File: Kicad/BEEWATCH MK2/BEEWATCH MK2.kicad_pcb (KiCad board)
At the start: 2 copper layers, 40.3 x 39.7 mm, 117 parts, among them IC1 LTC3549EDCB#TRMPBF, J1 USB_C_Receptacle_USB2.0, J3 Conn_02x06_Odd_Even, Q1 DMG6968U, Q2 DMG6968U, Q3 DMP1045U-7, Q4 DMG6968U, Q5 BSS138, Q6 BSS138, Q7 BSS138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

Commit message: minor changes
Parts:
- moved D1 6.40 mm to (168.7, 104.9), turned to 180 degrees
- moved R6 2.77 mm to (166.6, 105.0), turned to 90 degrees
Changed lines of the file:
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@@
 		(tags "SOT TO_SOT_SMD")
 		(property "Reference" "Q8"
-			(at -16.0375 -47.75 90)
+			(at 1.6 -2 90)
 			(layer "F.SilkS")
 			(effects
@@
 	(footprint "Resistor_SMD:R_0402_1005Metric_Pad0.72x0.64mm_HandSolder"
 		(layer "B.Cu")
-		(at 168.464645 107.05 180)
+		(at 166.6 105 90)
 		(descr "Resistor SMD 0402 (1005 Metric), square (rectangular) end terminal, IPC_7351 nominal with elongated pad for handsoldering. (Body size source: IPC-SM-782 page 72, https://www.pcb-3d.com/wordpress/wp-content/uploads/ipc-sm-782a_amendment_1_and_2.pdf), generated with kicad-footprint-generator")
 		(tags "resistor handsolder")
 		(property "Reference" "R6"
-			(at 0 1.17 0)
+			(at 0 1.17 90)
 			(layer "B.SilkS")
 			(effects
@@
 		)
 		(property "Value" "1K"
-			(at 0 -1.17 0)
+			(at 0 -1.17 90)
 			(layer "B.Fab")
 			(effects
@@
 		)
 		(property "Footprint" "Resistor_SMD:R_0402_1005Metric_Pad0.72x0.64mm_HandSolder"
-			(at 0 0 0)
+			(at 0 0 -90)
 			(unlocked yes)
 			(layer "B.Fab")
@@
 		)
 		(property "Datasheet" ""
-			(at 0 0 0)
+			(at 0 0 -90)
 			(unlocked yes)
 			(layer "B.Fab")
@@
 		)
 		(property "Description" "Resistor, small symbol"
-			(at 0 0 0)
+			(at 0 0 -90)
 			(unlocked yes)
 			(layer "B.Fab")
@@
 		(attr smd)
 		(fp_line
-			(start 0.167621 0.38)
-			(end -0.167621 0.38)
+			(start 0.167621 -0.380001)
+			(end -0.167621 -0.380001)
 			(stroke
 				(width 0.12)
@@
 		)
 		(fp_line
-			(start 0.167621 -0.38)
-			(end -0.167621 -0.38)
+			(start 0.167621 0.380001)
+			(end -0.167621 0.380001)
 			(stroke
 				(width 0.12)
@@
 		)
 		(fp_line
-			(start 1.1 0.47)
-			(end -1.1 0.47)
+			(start 1.1 -0.47)
+			(end 1.1 0.47)
 			(stroke
 				(width 0.05)
@@
 		)
 		(fp_line
-			(start 1.1 -0.47)
-			(end 1.1 0.47)
+			(start -1.1 -0.47)
+			(end 1.1 -0.47)
 			(stroke
 				(width 0.05)
@@
 		)
 		(fp_line
-			(start -1.1 0.47)
-			(end -1.1 -0.47)
+			(start 1.1 0.47)
+			(end -1.1 0.47)
 			(stroke
 				(width 0.05)
@@
 		)
 		(fp_line
-			(start -1.1 -0.47)
-			(end 1.1 -0.47)
+			(start -1.1 0.47)
+			(end -1.1 -0.47)
 			(stroke
 				(width 0.05)
@@
 		)
 		(fp_line
-			(start 0.525 0.27)
-			(end -0.525 0.27)
+			(start 0.525 -0.27)
+			(end 0.525 0.27)
 			(stroke
 				(width 0.1)
@@
 		)
 		(fp_line
-			(start 0.525 -0.27)
-			(end 0.525 0.27)
+			(start -0.525 -0.27)
+			(end 0.525 -0.27)
 			(stroke
 				(width 0.1)
@@
 		)
 		(fp_line
-			(start -0.525 0.27)
-			(end -0.525 -0.27)
+			(start 0.525 0.27)
+			(end -0.525 0.27)
 			(stroke
 				(width 0.1)
@@
 		)
 		(fp_line
-			(start -0.525 -0.27)
-			(end 0.525 -0.27)
+			(start -0.525 0.27)
+			(end -0.525 -0.27)
 			(stroke
 				(width 0.1)
@@
 		)
 		(fp_text user "${REFERENCE}"
-			(at 0 0 0)
+			(at 0 0 90)
 			(layer "B.Fab")
 			(effects
@@
 		)
 		(pad "1" smd roundrect
-			(at -0.5975 0 180)
+			(at -0.5975 0 90)
 			(size 0.715 0.64)
 			(layers "B.Cu" "B.Paste" "B.Mask")
@@
 		)
 		(pad "2" smd roundrect
-			(at 0.5975 0 180)
+			(at 0.5975 0 90)
 			(size 0.715 0.64)
 			(layers "B.Cu" "B.Paste" "B.Mask")
@@
 	(footprint "SM_LED:XL-0807RGBC-WS2812B"
 		(layer "B.Cu")
-		(at 167.1 111.1)
+		(at 168.7 104.9 180)
 		(property "Reference" "D1"
-			(at 0.5 1.7 180)
+			(at 0.5 1.7 0)
 			(unlocked yes)
 			(layer "B.SilkS")
@@
 		)
 		(property "Value" "WS2812B"
-			(at 0 -1 180)
+			(at 0 -1 0)
 			(unlocked yes)
 			(layer "B.Fab")
@@
 		)
 		(property "Footprint" "SM_LED:XL-0807RGBC-WS2812B"
-			(at 0 0 180)
+			(at 0 0 0)
 			(unlocked yes)
 			(layer "B.Fab")
@@
 		)
 		(property "Datasheet" "https://cdn-shop.adafruit.com/datasheets/WS2812B.pdf"
-			(at 0 0 180)
+			(at 0 0 0)
 			(unlocked yes)
 			(layer "B.Fab")
@@
 		)
 		(property "Description" "RGB LED with integrated controller"
-			(at 0 0 180)
+			(at 0 0 0)
 			(unlocked yes)
 			(layer "B.Fab")
@@
 		(attr smd)
 		(fp_line
-			(start 0.75 -0.9)
-			(end -0.75 -0.9)
+			(start 0.75 0.9)
+			(end -0.75 0.9)
 			(stroke
 				(width 0.1)
@@
 		)
 		(fp_line
-			(start 0.75 0.9)
-			(end -0.75 0.9)
+			(start 0.75 -0.9)
+			(end -0.75 -0.9)
 			(stroke
 				(width 0.1)
@@
 			(layer "B.SilkS")
 		)
-		(fp_rect
-			(start -1.15 1.05)
-			(end 1.15 -1.05)
+		(fp_poly
+			(pts
+				(xy -1.15 1.05) (xy 1.15 1.05) (xy 1.15 -1.05) (xy -1.15 -1.05)
+			)
 			(stroke
 				(width 0.05)
@@
 		)
 		(fp_text user "${REFERENCE}"
-			(at 0 -2.5 180)
+			(at 0 -2.5 0)
 			(unlocked yes)
 			(layer "B.Fab")
@@
 		)
 		(pad "1" smd roundrect
-			(at 0.75 0.45)
+			(at 0.75 0.45 180)
 			(size 0.6 0.7)
 			(layers "B.Cu" "B.Paste" "B.Mask")
@@
 		)
 		(pad "2" smd roundrect
-			(at -0.75 0.45)
+			(at -0.75 0.45 180)
 			(size 0.6 0.7)
 			(layers "B.Cu" "B.Paste" "B.Mask")
@@
 		)
 		(pad "3" smd roundrect
-			(at -0.75 -0.45)
+			(at -0.75 -0.45 180)
 			(size 0.6 0.7)
 			(layers "B.Cu" "B.Paste" "B.Mask")
@@
 		)
 		(pad "4" smd roundrect
-			(at 0.75 -0.45)
+			(at 0.75 -0.45 180)
 			(size 0.6 0.7)
 			(layers "B.Cu" "B.Paste" "B.Mask")
@@
 			(pintype "input")
 		)
-		(model "/home/krishnawa/git/BEEWATCH/3D/LED/XL-0807RGBC-WS2812B.step"
+		(model "${KIPRJMOD}/KiCadoodle/LIB/SM_LED/3D/0807RGB/XL-0807RGBC-WS2812B.step"
 			(offset
 				(xyz 0 0 0)
@@
 			(pintype "passive")
 		)
-		(model "/home/krishnawa/git/BEEWATCH/3D/SWITCH/Tact Switch-TK-074-4 Pin SMD.step"
+		(model "${KIPRJMOD}/KiCadoodle/LIB/SM_SWITCH/3D/TK-074/Tact Switch-TK-074-4 Pin SMD.step"
 			(offset
 				(xyz 0 0 0)
@@
 			(pintype "passive")
 		)
-		(model "/home/krishnawa/git/BEEWATCH/3D/SWITCH/Tact Switch-TK-074-4 Pin SMD.step"
+		(model "${KIPRJMOD}/KiCadoodle/LIB/SM_SWITCH/3D/TK-074/Tact Switch-TK-074-4 Pin SMD.step"
 			(offset
 				(xyz 0 0 0)

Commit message: Update
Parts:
- moved R22 11.5 mm to (133.8, 100.8), turned to 0 degrees
- moved R21 9.19 mm to (133.8, 102.2), turned to 0 degrees
- moved R2 8.52 mm to (139.9, 103.3), turned to 0 degrees
- moved R1 8.03 mm to (139.9, 106.3), turned to 0 degrees
- moved R20 3.82 mm to (137.4, 102.0), turned to 0 degrees
- moved R37 2.06 mm to (149.2, 98.4), turned to 0 degrees
- moved R36 0.30 mm to (145.9, 99.5)
- moved C22 0.21 mm to (132.8, 97.8)
- moved R43 0.20 mm to (140.9, 97.2)
- moved C23 0.19 mm to (134.3, 97.8)
- moved R33 0.18 mm to (141.7, 102.9)
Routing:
- net VBUS: track 0.00 -> 25.5 mm
- net /Battery&BMS/VBAT: track 0.00 -> 19.3 mm
- net /Battery&BMS/+VBAT_IN: track 0.00 -> 12.6 mm
- net GND: track 0.00 -> 10.6 mm, vias 0 -> 3
- net +3.3V: track 0.00 -> 5.57 mm, vias 0 -> 2
- net Net-(J1-CC1): track 0.00 -> 4.02 mm
- net Net-(U4-STAT): track 0.00 -> 3.17 mm
- net /ESP32/D+: track 0.00 -> 2.83 mm
- net /ESP32/D-: track 0.00 -> 2.78 mm
- net Net-(J1-CC2): track 0.00 -> 2.70 mm
- net /ESP32/XTAL_32K_P: track 0.00 -> 1.11 mm
- net /Battery&BMS/+3V3_IN: track 0.00 -> 0.99 mm
- added copper zone on In2.Cu, net +3.3V
- added copper zone on In1.Cu, net GND
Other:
- copper layers 2 -> 4

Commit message: ERC Checking
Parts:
- moved R23 1.49 mm to (154.7, 113.6)
- moved Y1 0.13 mm to (155.1, 116.0), turned to -45 degrees
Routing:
- net Net-(U1-GPIO46): track 0.00 -> 10.9 mm, vias 0 -> 2
- net Net-(U1-GPIO45): track 0.00 -> 9.92 mm, vias 0 -> 2
- net /ESP32/U1TXD: track 0.00 -> 9.46 mm, vias 0 -> 2
- net /ESP32/U1RXD: track 0.00 -> 6.76 mm, vias 0 -> 2
- net /ESP32/XTAL_P: track 0.00 -> 5.26 mm
- net /ESP32/XTAL_N: track 0.50 -> 5.34 mm
- net /ACCELEROMETER/MPU_SDA: track 0.00 -> 4.46 mm
- net 3V3: track 0.00 -> 4.38 mm
- net /ESP32/XTAL_32K_N: track 0.00 -> 4.38 mm
- net /ESP32/USB_D+: track 0.00 -> 3.97 mm
- net /ESP32/USB_D-: track 0.00 -> 3.94 mm
- net VDD3P3_RTC: track 0.00 -> 3.53 mm
- net /ESP32/D-: track 2.78 -> 0.00 mm
- net /ESP32/XTAL_32K_P: track 1.11 -> 3.34 mm
- net /ACCELEROMETER/MPU_SCL: track 0.00 -> 2.01 mm
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
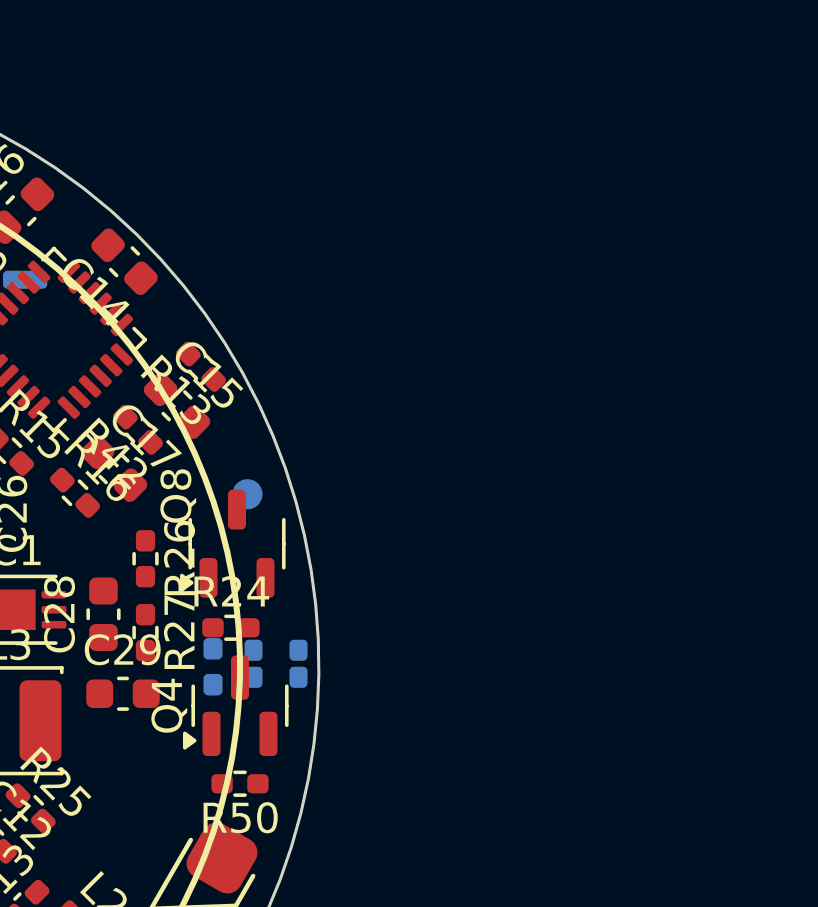
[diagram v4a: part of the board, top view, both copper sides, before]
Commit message: ERC going on anf All Lib issue is fixed
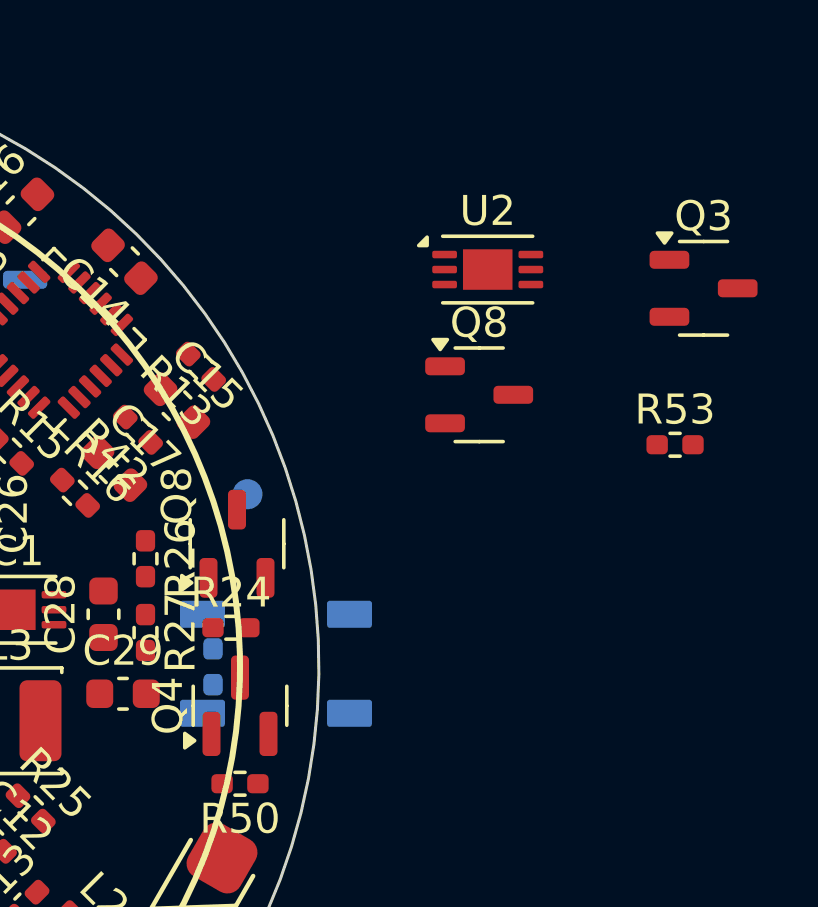
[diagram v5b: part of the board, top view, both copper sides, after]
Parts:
- added Q3: DMP1045U-7, Package_TO_SOT_SMD:SOT-23-3, F.Cu at (183.0, 92.4)
- added Q8: DMP1045U-7, Package_TO_SOT_SMD:SOT-23-3, F.Cu at (175.5, 95.9)
- added R53: 0, Resistor_SMD:R_0402_1005Metric_Pad0.72x0.64mm_HandSolder, F.Cu at (182.0, 97.6)
- added U2: LTC3549EDCB#TRMPBF, Package_DFN_QFN:DFN-6-1EP_3x2mm_P0.5mm_EP1.65x1.35mm, F.Cu at (175.8, 91.8)
- D1: footprint SM_LED:XL-0807RGBC-WS2812B -> LED_SMD:LED_WS2812B_PLCC4_5.0x5.0mm_P3.2mm
- R34: value K10K -> 10K
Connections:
- BZ1 pad 1: +VBAT -> Net-(BZ1-+)
- C28 pad 2: Net-(IC1-VFB) -> Net-(U2-VFB)
- D1 pad 4: Net-(D1-DIN) -> /ESP32/LED1
- D4 pad 1: +VBAT -> Net-(BZ1-+)
- L3 pad 1: Net-(IC1-SW) -> Net-(U2-SW)
- R26 pad 2: Net-(IC1-VFB) -> Net-(U2-VFB)
- R27 pad 1: Net-(IC1-VFB) -> Net-(U2-VFB)
- R6 pad 1: Net-(D1-DIN) -> /ESP32/LED1

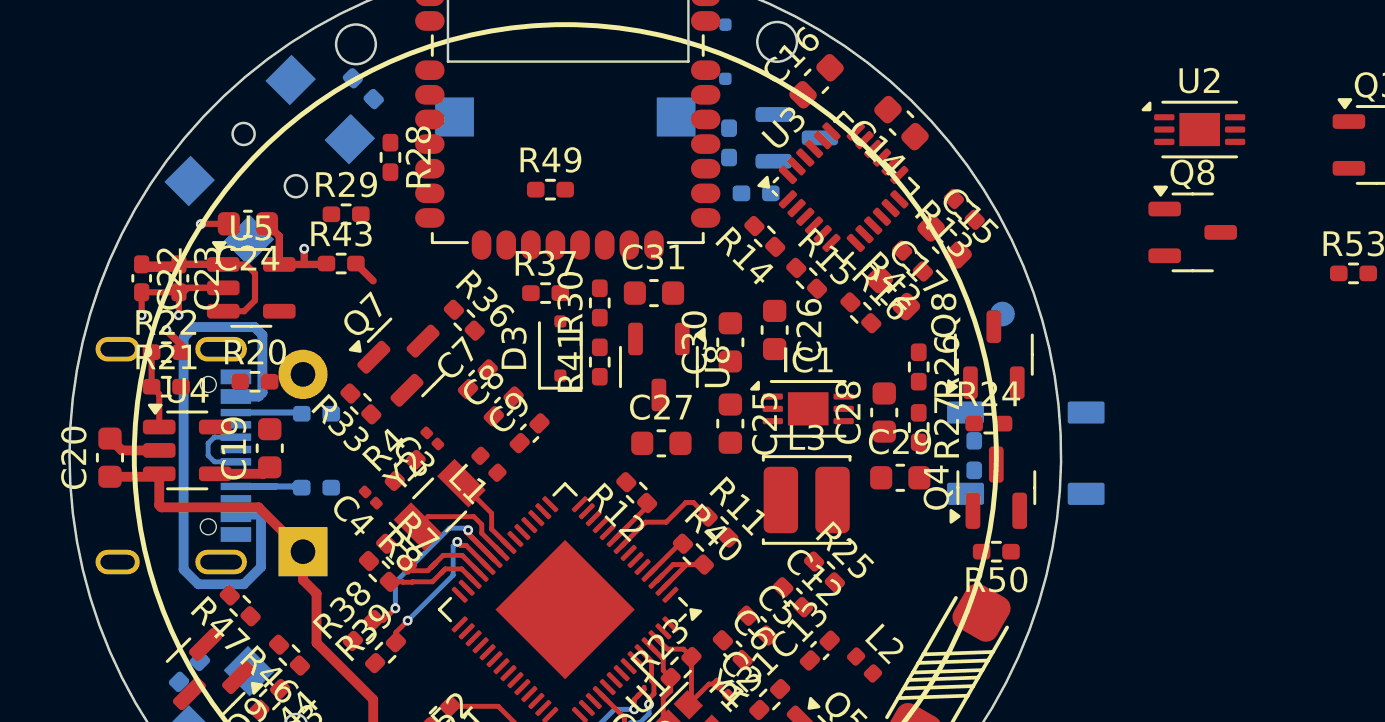
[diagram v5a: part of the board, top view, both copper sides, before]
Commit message: Pending task Crystal footprint
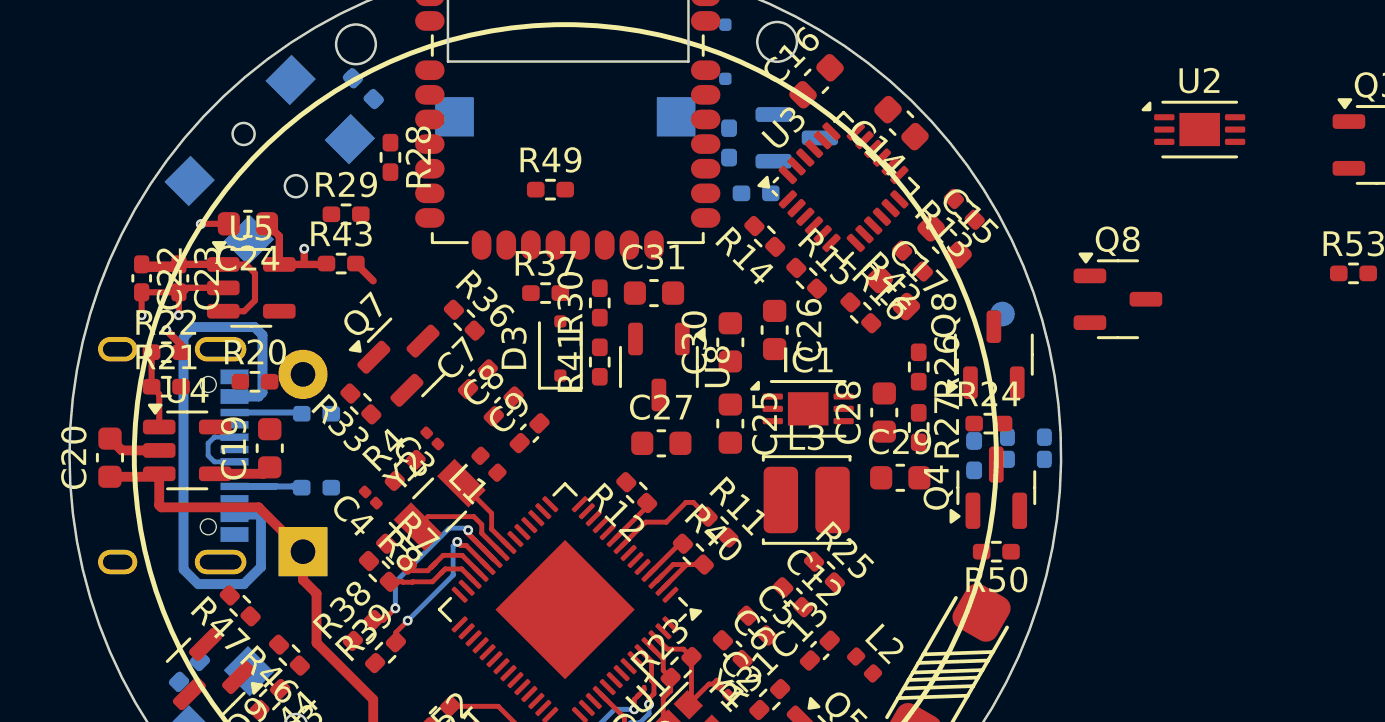
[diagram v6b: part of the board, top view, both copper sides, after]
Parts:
- D1: value WS2812B -> WS2812B-0807; footprint LED_SMD:LED_WS2812B_PLCC4_5.0x5.0mm_P3.2mm -> SM_LED:XL-0807RGBC-WS2812B
- J1: value USB_C_Receptacle_USB2.0 -> USB_C_Receptacle_USB2.0_16P; footprint Connector_USB:USB_C_Receptacle_G-Switch_GT-USB-7010ASV -> Connector_USB:USB_C_Receptacle_XKB_U262-16XN-4BVC11
- moved Q8 4.07 mm to (172.4, 98.7)
- moved D1 0.20 mm to (168.7, 104.7), turned to 0 degrees
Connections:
- net /ESP32/U1RXD renamed /ESP32/GPS_RXD
- net /ESP32/U1TXD renamed /ESP32/GPS_TXD
- D1 pad 2: unconnected-(D1-DOUT-Pad2) -> /ESP32/LED1
- D1 pad 4: /ESP32/LED1 -> unconnected-(D1-DIN-Pad4)
- R9 pad 1: D3 -> /ESP32/BUZZER_EN

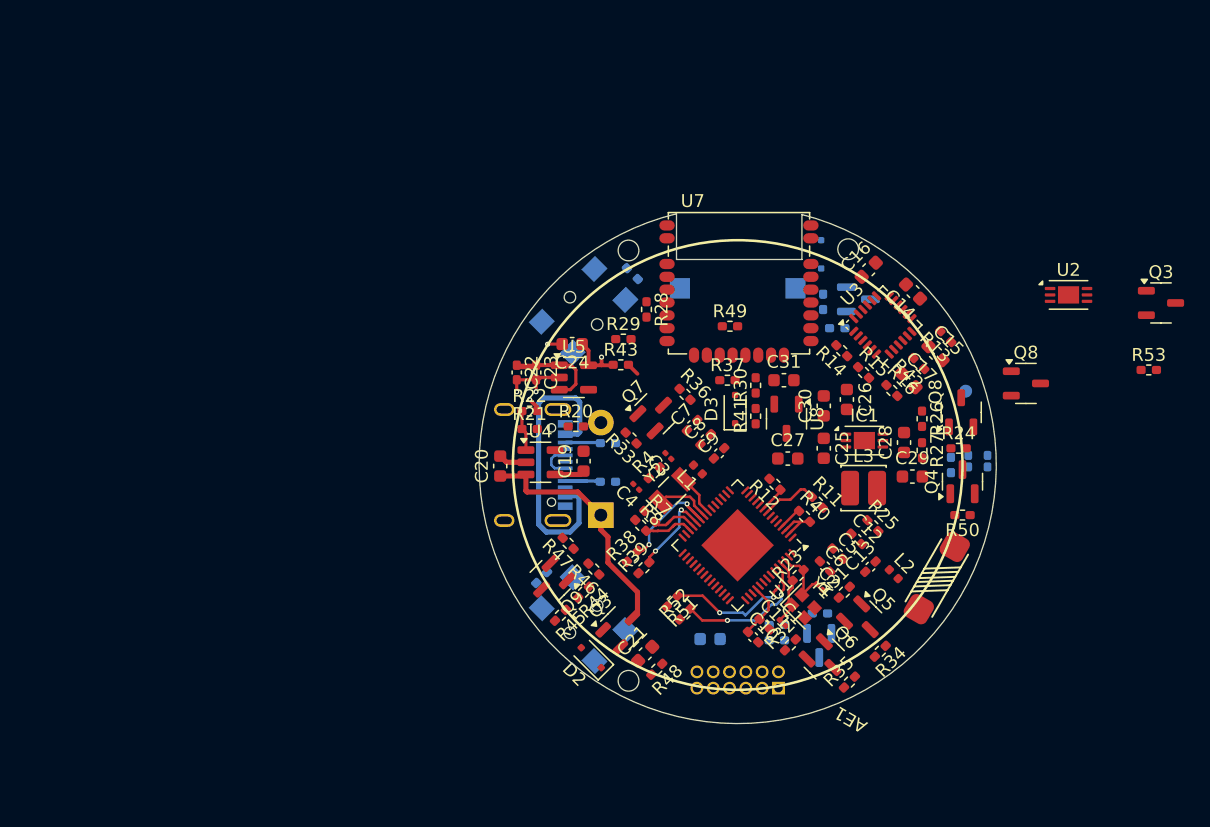
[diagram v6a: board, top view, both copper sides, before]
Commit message: Crystal footprint fixed
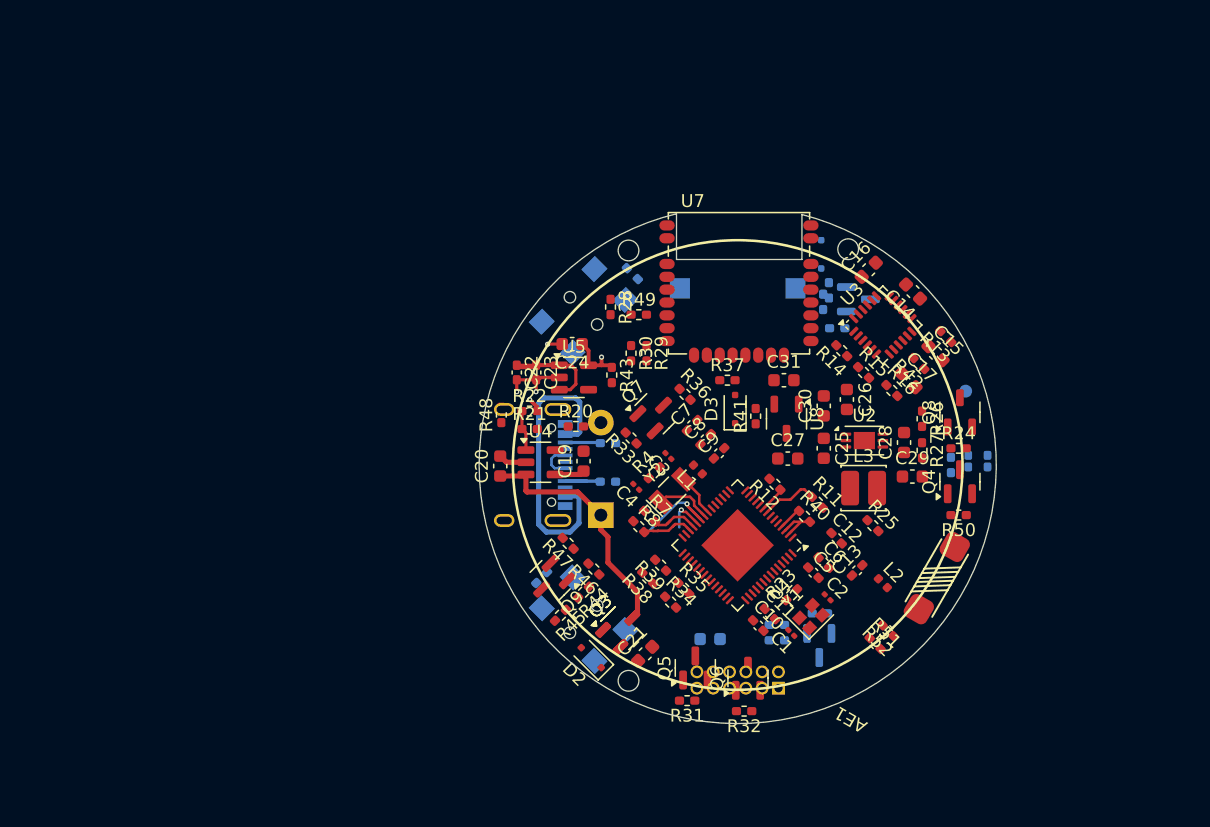
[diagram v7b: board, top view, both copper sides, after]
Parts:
- removed IC1: LTC3549EDCB#TRMPBF, Package_DFN_QFN:DFN-6-1EP_3x2mm_P0.5mm_EP1.65x1.35mm
- removed the Q8 at (167.4, 100.9)
- R53: moved to B.Cu
- moved Q3 49.0 mm to (141.0, 117.7), turned to 45 degrees
- moved R53 25.7 mm to (157.1, 91.4), turned to 90 degrees
- moved R48 23.2 mm to (131.6, 101.1), turned to 90 degrees
- moved U2 19.5 mm to (159.9, 103.1)
- moved R34 16.8 mm to (144.8, 115.7), turned to -45 degrees
- moved R51 16.1 mm to (160.7, 118.9), turned to -45 degrees
- moved R52 15.9 mm to (161.7, 117.9), turned to 135 degrees
- moved R31 14.9 mm to (146.1, 123.3), turned to 180 degrees
- moved R35 14.8 mm to (145.8, 114.6), turned to -45 degrees
- moved Q5 13.5 mm to (146.7, 120.8), turned to 90 degrees
- moved R30 10.0 mm to (141.7, 96.3), turned to -90 degrees
- moved R49 7.15 mm to (142.3, 93.3)
- moved R32 6.29 mm to (150.5, 124.2), turned to 180 degrees
- moved Q6 6.12 mm to (150.8, 121.6), turned to 90 degrees
- moved Q8 5.61 mm to (167.3, 100.9), turned to 90 degrees
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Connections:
- Y1 pad 3: GND -> /ESP32/XTAL_P
- Y1 pad 4: /ESP32/XTAL_P -> GND
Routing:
- net Net-(U1-GPIO46): track 10.9 -> 0.00 mm, vias 2 -> 0
- net Net-(U1-GPIO45): track 9.92 -> 0.00 mm, vias 2 -> 0
- net /ESP32/XTAL_N: track 5.34 -> 0.00 mm
- net /ESP32/XTAL_P: track 5.26 -> 0.00 mm
- net 3V3: track 4.38 -> 0.00 mm
- net /ESP32/GPS_RXD: track 6.76 -> 3.07 mm, vias 2 -> 1
- net /ESP32/GPS_TXD: track 9.46 -> 7.32 mm, vias 2 -> 1
- net /Battery&BMS/+3V3_IN: track 0.99 -> 0.00 mm
